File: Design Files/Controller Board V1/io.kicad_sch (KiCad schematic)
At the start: 8 parts, among them J1 XT30PW-M, J2 XT30PW-M, J3 XT30PW-M, J4 XT30PW-M, J5 XT30PW-M, J6 XT30PW-M, J7 XT30PW-F, J8 SM04B-GHS-TB_LF__SN_-

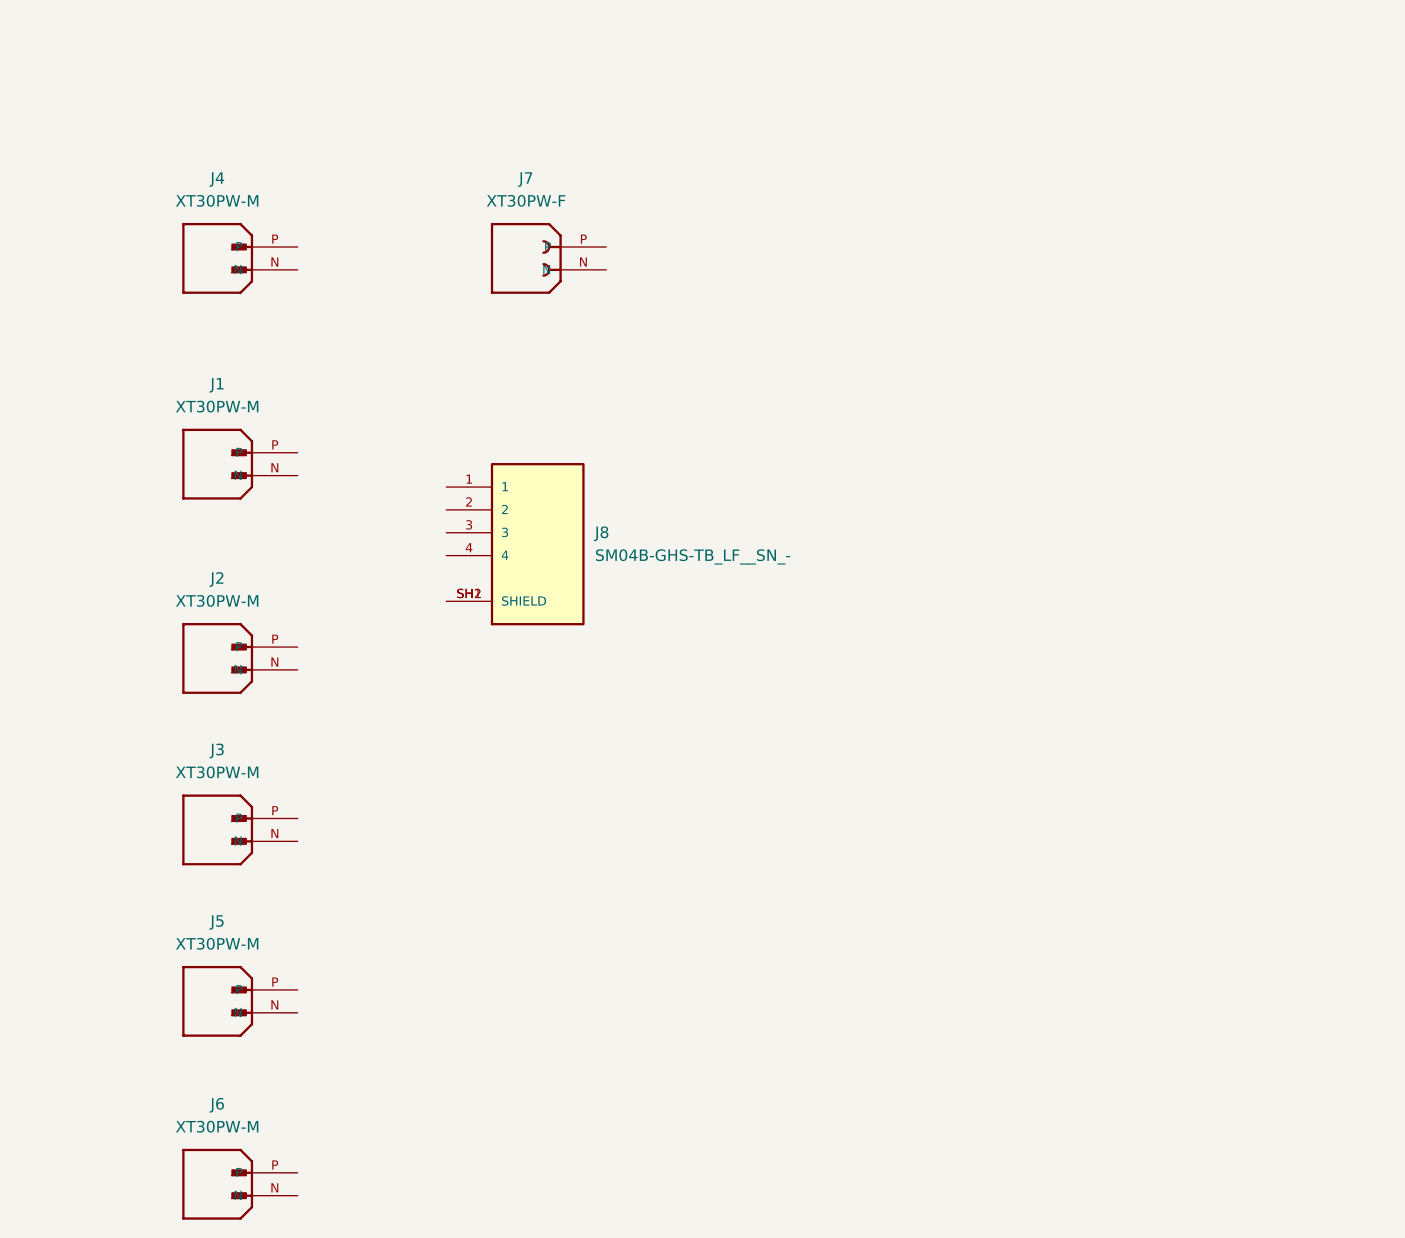
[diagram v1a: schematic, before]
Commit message: Pico Schematic Started
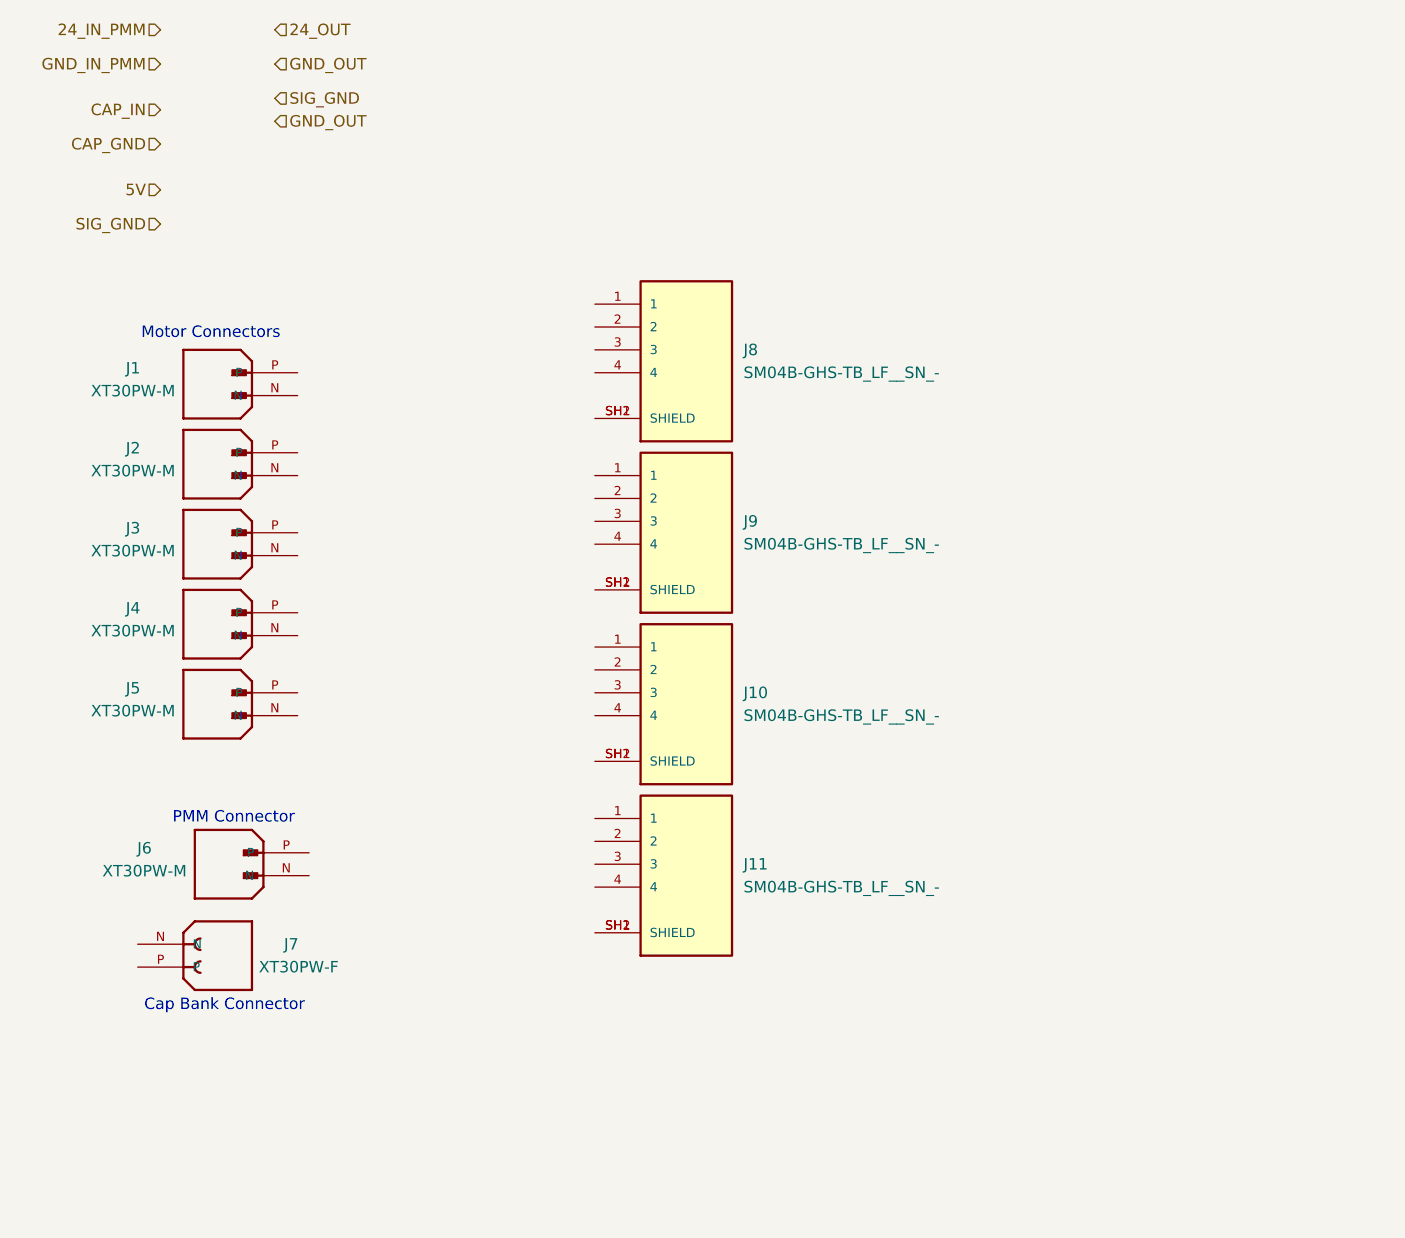
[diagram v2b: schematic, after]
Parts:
- added J10, J11, J9: SM04B-GHS-TB_LF__SN_-, SM04B-GHS-TB_LF__SN_-:JST_SM04B-GHS-TB_LF__SN_-, symbol SM04B-GHS-TB_LF__SN_-:SM04B-GHS-TB_LF__SN_-
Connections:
- new net: J10.SH1 (SHIELD), J10.SH2 (SHIELD)
- new net: J11.SH1 (SHIELD), J11.SH2 (SHIELD)
- new net: J9.SH1 (SHIELD), J9.SH2 (SHIELD)
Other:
- note added: "Cap Bank Connector"
- note added: "Motor Connectors"
- note added: "PMM Connector"
- moved on the sheet: J1, J7, J8

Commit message: Assigning footprints and ading to schematic
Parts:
- J1: renamed from J7; footprint XT30PW-F:AMASS_XT30PW-F -> PassiveBankV1:XT30PW-F
- J2: renamed from J1; footprint XT30PW-M:AMASS_XT30PW-M -> PassiveBankV1:XT30PW-M
- J3: renamed from J2; footprint XT30PW-M:AMASS_XT30PW-M -> PassiveBankV1:XT30PW-M
- J4: renamed from J3; footprint XT30PW-M:AMASS_XT30PW-M -> PassiveBankV1:XT30PW-M
- J5: renamed from J4; footprint XT30PW-M:AMASS_XT30PW-M -> PassiveBankV1:XT30PW-M
- J6: renamed from J5; footprint XT30PW-M:AMASS_XT30PW-M -> PassiveBankV1:XT30PW-M
- J7: renamed from J6; footprint XT30PW-M:AMASS_XT30PW-M -> PassiveBankV1:XT30PW-M
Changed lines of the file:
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@@
 		(shape input)
 		(at 64.77 21.59 0)
-		(fields_autoplaced yes)
 		(effects
 			(font
@@
 		(shape input)
 		(at 64.77 17.78 0)
-		(fields_autoplaced yes)
 		(effects
 			(font
@@
 		(shape input)
 		(at 64.77 25.4 0)
-		(fields_autoplaced yes)
 		(effects
 			(font
@@
 		(shape input)
 		(at 64.77 27.94 0)
-		(fields_autoplaced yes)
 		(effects
 			(font
@@
 		(shape input)
 		(at 52.07 39.37 180)
-		(fields_autoplaced yes)
 		(effects
 			(font
@@
 		(shape input)
 		(at 52.07 21.59 180)
-		(fields_autoplaced yes)
 		(effects
 			(font
@@
 		(shape input)
 		(at 52.07 26.67 180)
-		(fields_autoplaced yes)
 		(effects
 			(font
@@
 		(shape input)
 		(at 52.07 30.48 180)
-		(fields_autoplaced yes)
 		(effects
 			(font
@@
 		(shape input)
 		(at 52.07 35.56 180)
-		(fields_autoplaced yes)
 		(effects
 			(font
@@
 		(shape input)
 		(at 52.07 17.78 180)
-		(fields_autoplaced yes)
 		(effects
 			(font
@@
 		(on_board yes)
 		(dnp no)
-		(property "Reference" "J3"
+		(property "Reference" "J4"
 			(at 49.022 73.152 0)
 			(effects
@@
 			)
 		)
-		(property "Footprint" "XT30PW-M:AMASS_XT30PW-M"
+		(property "Footprint" "PassiveBankV1:XT30PW-M"
 			(at 62.23 73.66 0)
 			(effects
@@
 			(project "Control Board V1"
 				(path "/e0c606b8-cbb9-4aff-b96c-73876da6ca74/ba5c2d63-7c4b-497a-9de4-bddeb8ed5de8"
-					(reference "J3")
+					(reference "J4")
 					(unit 1)
 				)
@@
 		(on_board yes)
 		(dnp no)
-		(property "Reference" "J5"
+		(property "Reference" "J6"
 			(at 49.022 90.932 0)
 			(effects
@@
 			)
 		)
-		(property "Footprint" "XT30PW-M:AMASS_XT30PW-M"
+		(property "Footprint" "PassiveBankV1:XT30PW-M"
 			(at 62.23 91.44 0)
 			(effects
@@
 			(project "Control Board V1"
 				(path "/e0c606b8-cbb9-4aff-b96c-73876da6ca74/ba5c2d63-7c4b-497a-9de4-bddeb8ed5de8"
-					(reference "J5")
+					(reference "J6")
 					(unit 1)
 				)
@@
 		(on_board yes)
 		(dnp no)
-		(property "Reference" "J2"
+		(property "Reference" "J3"
 			(at 49.022 64.262 0)
 			(effects
@@
 			)
 		)
-		(property "Footprint" "XT30PW-M:AMASS_XT30PW-M"
+		(property "Footprint" "PassiveBankV1:XT30PW-M"
 			(at 62.23 64.77 0)
 			(effects
@@
 			(project "Control Board V1"
 				(path "/e0c606b8-cbb9-4aff-b96c-73876da6ca74/ba5c2d63-7c4b-497a-9de4-bddeb8ed5de8"
-					(reference "J2")
+					(reference "J3")
 					(unit 1)
 				)
@@
 		(on_board yes)
 		(dnp no)
-		(property "Reference" "J6"
+		(property "Reference" "J7"
 			(at 50.292 108.712 0)
 			(effects
@@
 			)
 		)
-		(property "Footprint" "XT30PW-M:AMASS_XT30PW-M"
+		(property "Footprint" "PassiveBankV1:XT30PW-M"
 			(at 63.5 109.22 0)
 			(effects
@@
 			(project "Control Board V1"
 				(path "/e0c606b8-cbb9-4aff-b96c-73876da6ca74/ba5c2d63-7c4b-497a-9de4-bddeb8ed5de8"
-					(reference "J6")
+					(reference "J7")
 					(unit 1)
 				)
@@
 		(on_board yes)
 		(dnp no)
-		(property "Reference" "J1"
+		(property "Reference" "J2"
 			(at 49.022 55.372 0)
 			(effects
@@
 			)
 		)
-		(property "Footprint" "XT30PW-M:AMASS_XT30PW-M"
+		(property "Footprint" "PassiveBankV1:XT30PW-M"
 			(at 62.23 55.88 0)
 			(effects
@@
 			(project "Control Board V1"
 				(path "/e0c606b8-cbb9-4aff-b96c-73876da6ca74/ba5c2d63-7c4b-497a-9de4-bddeb8ed5de8"
-					(reference "J1")
+					(reference "J2")
 					(unit 1)
 				)
@@
 		(on_board yes)
 		(dnp no)
-		(property "Reference" "J4"
+		(property "Reference" "J5"
 			(at 49.022 82.042 0)
 			(effects
@@
 			)
 		)
-		(property "Footprint" "XT30PW-M:AMASS_XT30PW-M"
+		(property "Footprint" "PassiveBankV1:XT30PW-M"
 			(at 62.23 82.55 0)
 			(effects
@@
 			(project "Control Board V1"
 				(path "/e0c606b8-cbb9-4aff-b96c-73876da6ca74/ba5c2d63-7c4b-497a-9de4-bddeb8ed5de8"
-					(reference "J4")
+					(reference "J5")
 					(unit 1)
 				)
@@
 		(on_board yes)
 		(dnp no)
-		(property "Reference" "J7"
+		(property "Reference" "J1"
 			(at 65.786 119.38 0)
 			(effects
@@
 			)
 		)
-		(property "Footprint" "XT30PW-F:AMASS_XT30PW-F"
+		(property "Footprint" "PassiveBankV1:XT30PW-F"
 			(at 54.61 121.92 0)
 			(effects
@@
 			(project "Control Board V1"
 				(path "/e0c606b8-cbb9-4aff-b96c-73876da6ca74/ba5c2d63-7c4b-497a-9de4-bddeb8ed5de8"
-					(reference "J7")
+					(reference "J1")
 					(unit 1)
 				)

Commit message: yay(meeting 2/16/2025)
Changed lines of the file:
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@@
 	(hierarchical_label "GND_OUT"
 		(shape input)
-		(at 64.77 27.94 0)
+		(at 64.77 29.21 0)
 		(effects
 			(font

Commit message: Major Schematic Progress
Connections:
- net 24_IN_PMM: now also J7.P
- net 5V: now also J10.1, J11.1, J9.1
- net CAP_IN: now also J1.P
- net GPIO_3: now reaches J10.2
- net GPIO_2: now reaches J10.3
- net D_GND: now reaches J10.4
- net D_GND: now also J11.4, J8.2, J8.4, J9.4
- net GPIO_1: now reaches J11.2
- net GPIO_0: now reaches J11.3
- net P_GND: now reaches J4.N
- net P_GND: now also J1.N, J2.N, J3.N, J5.N, J6.N, J7.N
- net 24V_OUT: now reaches J4.P
- net 24V_OUT: now also J2.P, J3.P, J5.P, J6.P
- net GPIO_5: now reaches J9.2
- net GPIO_4: now reaches J9.3
- net I2C_TypeC_SDA: now reaches J8.1
- net I2C_TypeC_SCL: now reaches J8.3
- no-connect marks 0 -> 4
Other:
- moved on the sheet: J1, J10, J11, J2, J3, J4, J5, J6, J7, J8, J9

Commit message: general layout revised
goodnight
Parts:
- added C10, C11, C7, C8, C9: 10u, Capacitor_SMD:C_0603_1608Metric, symbol Device:C
- J2, J3, J4, J5, J6, J7: value XT30PW-M -> XT30UPB-M; footprint PassiveBankV1:XT30PW-M -> Connector_AMASS:AMASS_XT30UPB-M_1x02_P5.0mm_Vertical
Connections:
- net 24V_OUT: now also C10.2, C7.2, C8.2, C9.2
- net 24_IN_PMM: now also C11.2
- net P_GND: now also C10.1, C11.1, C7.1, C8.1, C9.1
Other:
- moved on the sheet: J1, J2, J3, J4, J5, J6, J7

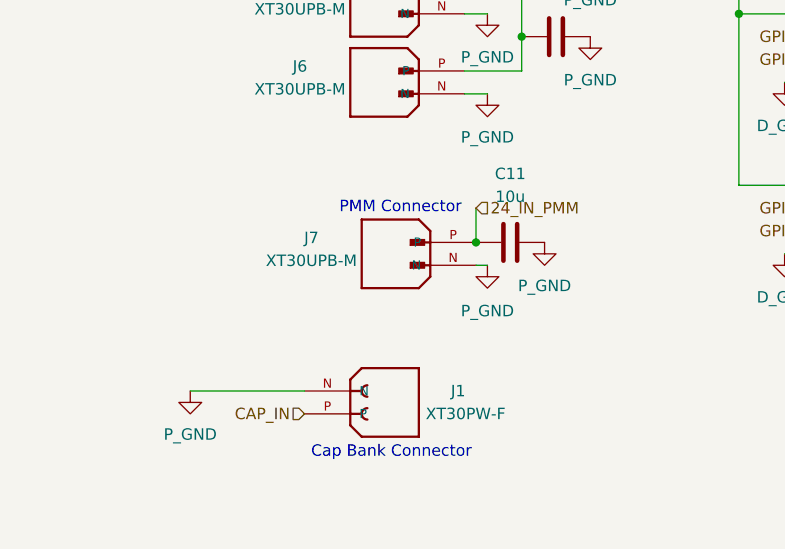
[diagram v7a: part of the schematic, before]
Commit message: Changed to four layer and added pours
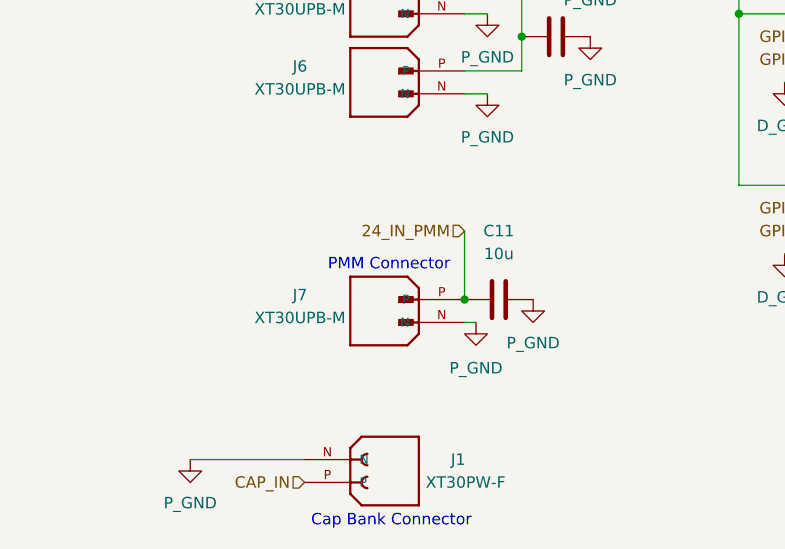
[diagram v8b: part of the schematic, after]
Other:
- moved on the sheet: C11, J1, J7
